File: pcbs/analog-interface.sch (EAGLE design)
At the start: 26 parts, among them U1 ISL3179EIBZ, U2 ATMEGA328P, U3 LM4120

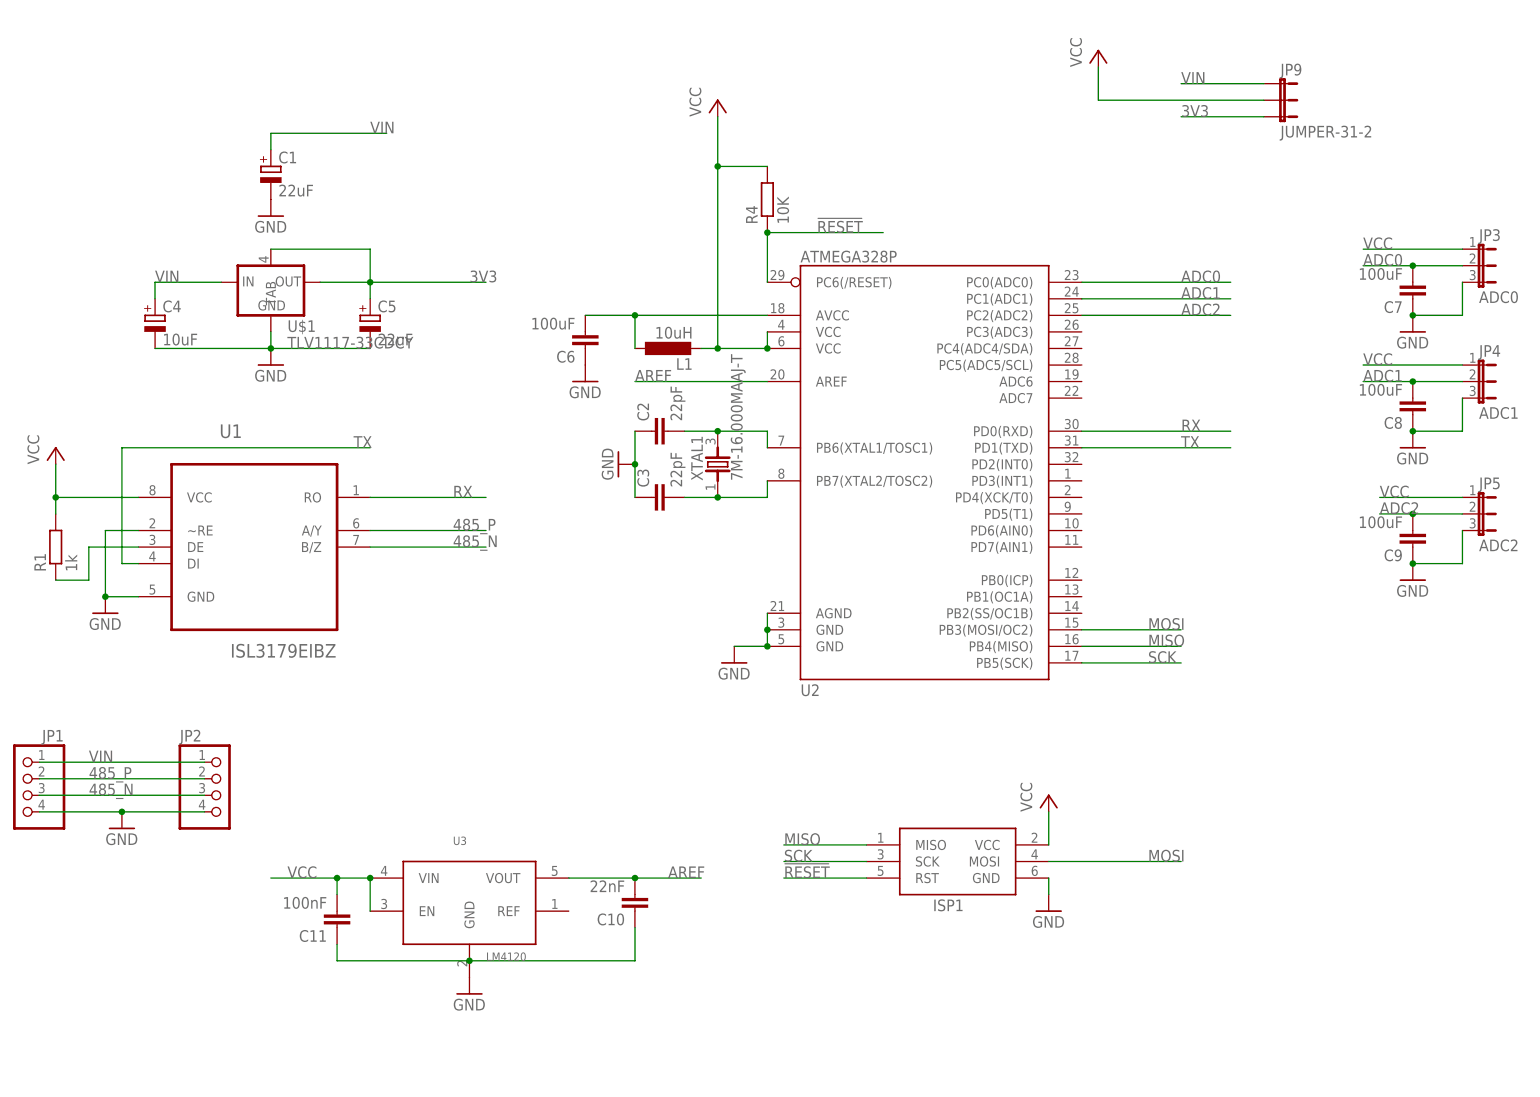
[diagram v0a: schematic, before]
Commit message: Now uses external ADC and is long and thin.  Possibly too long...
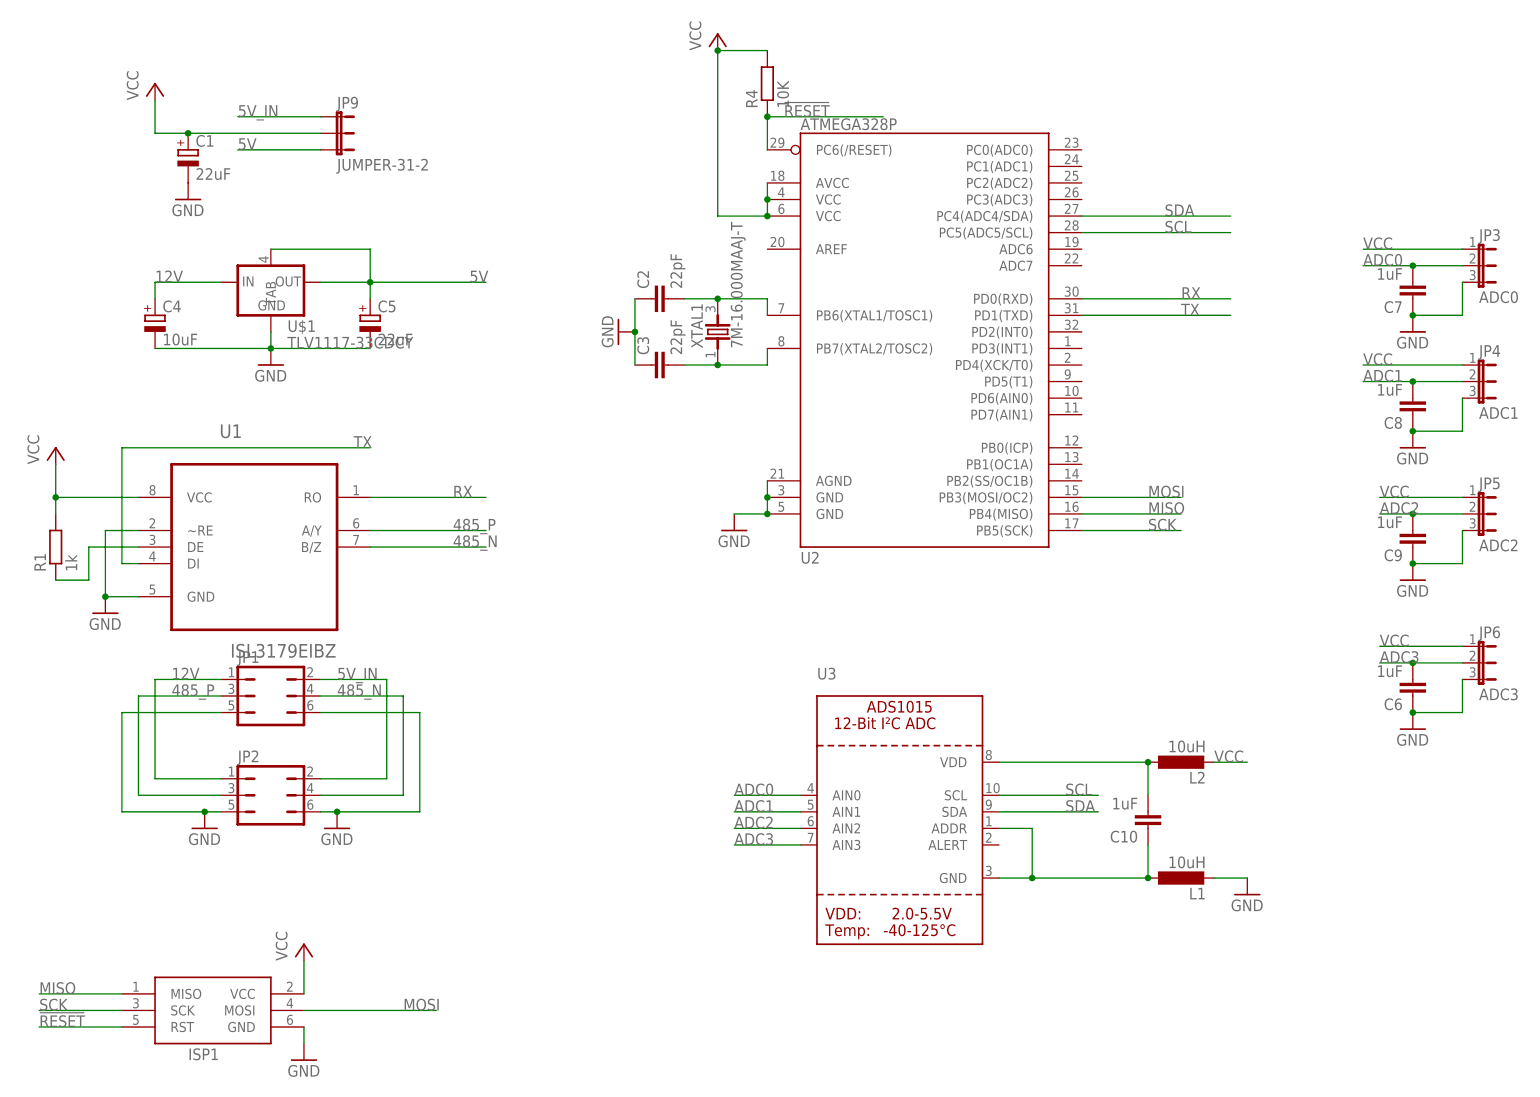
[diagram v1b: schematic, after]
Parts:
- removed C11: 100nF, resistor:C-EUC0805
- added JP6: ADC3, jumper:JP2E
- added L2: 10uH, resistor:L-EUL3216C
- C10: value 22nF -> 1uF
- C6, C7, C8, C9: value 100uF -> 1uF
- JP1, JP2: device pinhead:PINHD-1X4 -> jumper:JP3Q
- JP3, JP4, JP5: device farnell-parts:3-PIN-MOLEX -> jumper:JP2E
- U3: value LM4120 -> (none); device mountainsensing:LM4120 -> microbuilder:ADC_ADS1015
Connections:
- net 3V3 renamed 5V
- removed net AREF: C10.2, U2.AREF, U3.VOUT
- removed net VIN: C1.+, C4.+, JP1.1, JP2.1, JP9.1, U$1.IN
- new net 12V: C4.+, JP1.1, JP2.1, U$1.IN
- new net 5V_IN: JP1.2, JP2.2, JP9.1
- new net ADC3: C6.2, JP6.2, U3.AIN3
- new net SCL: U2.PC5(ADC5/SCL), U3.SCL
- new net SDA: U2.PC4(ADC4/SDA), U3.SDA
- net 485_N: now also JP1.4, JP2.4; no longer JP1.3, JP2.3
- net 485_P: now also JP1.3, JP2.3; no longer JP1.2, JP2.2
- net ADC0: now also U3.AIN0; no longer U2.PC0(ADC0)
- net ADC1: now also U3.AIN1; no longer U2.PC1(ADC1)
- net ADC2: now also U3.AIN2; no longer U2.PC2(ADC2)
- net GND: now also JP1.5, JP1.6, JP2.5, JP2.6, JP6.3, L1.2; no longer JP1.4, JP2.4, U3.GND
- net N$4: now also C10.1, U3.ADDR, U3.GND; no longer C6.2, U2.AVCC
- net N$7: now also C10.2, L2.1, U3.VDD; no longer C10.1, C11.1
- net VCC: now also C1.+, JP6.1, L2.2, U2.AVCC; no longer C11.2, L1.2, U3.EN, U3.VIN
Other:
- moved on the sheet: C1, C10, C2, C3, C6, ISP1, JP9, L1, R4, U2, XTAL1

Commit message: Now has seperate AGND and AVCC 12V available on ADC headers lots of vias A bit shorter
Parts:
- removed JP1, JP2: (no value), jumper:JP3Q
- added JP7, JP8: (no value), SparkFun-Connectors:M05PTH
- JP3: value ADC0 -> 0; device jumper:JP2E -> jumper:JP4E
- JP4: value ADC1 -> 1; device jumper:JP2E -> jumper:JP4E
- JP5: value ADC2 -> 2; device jumper:JP2E -> jumper:JP4E
- JP6: value ADC3 -> 3; device jumper:JP2E -> jumper:JP4E
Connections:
- removed net 12V: C4.+, JP1.1, JP2.1, U$1.IN
- removed net N$4: C10.1, L1.1, U3.ADDR, U3.GND
- removed net N$7: C10.2, L2.1, U3.VDD
- new net 12V_IN: C4.+, JP3.1, JP4.1, JP5.1, JP6.1, JP7.1, JP8.1, U$1.IN
- new net AGND: C10.1, C6.1, C7.1, C8.1, C9.1, JP3.4, JP4.4, JP5.4, JP6.4, L1.1, U3.ADDR, U3.GND
- new net AVCC: C10.2, JP3.2, JP4.2, JP5.2, JP6.2, L2.1, U3.VDD
- net 485_N: now also JP7.4, JP8.4; no longer JP1.4, JP2.4
- net 485_P: now also JP7.3, JP8.3; no longer JP1.3, JP2.3
- net 5V_IN: now also JP7.2, JP8.2; no longer JP1.2, JP2.2
- net ADC0: now also JP3.3; no longer JP3.2
- net ADC1: now also JP4.3; no longer JP4.2
- net ADC2: now also JP5.3; no longer JP5.2
- net ADC3: now also JP6.3; no longer JP6.2
- net GND: now also JP7.5, JP8.5; no longer C6.1, C7.1, C8.1, C9.1, JP1.5, JP1.6, JP2.5, JP2.6, JP3.3, JP4.3, JP5.3, JP6.3
- net VCC: no longer JP3.1, JP4.1, JP5.1, JP6.1
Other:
- moved on the sheet: C7, C8

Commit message: Pull ups added to I2C
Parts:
- added R2, R3: 1k, resistor:R-EU_R0805
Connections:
- net SCL: now also R2.1
- net SDA: now also R3.1
- net VCC: now also R2.2, R3.2
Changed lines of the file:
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@@
 <?xml version="1.0" encoding="utf-8"?>
 <!DOCTYPE eagle SYSTEM "eagle.dtd">
-<eagle version="6.6.0">
+<eagle version="6.5.0">
 <drawing>
 <settings>
@@
 <part name="JP8" library="SparkFun-Connectors" deviceset="M05" device="PTH"/>
 <part name="GND6" library="supply1" deviceset="GND" device=""/>
+<part name="R2" library="resistor" deviceset="R-EU_" device="R0805" value="1k"/>
+<part name="R3" library="resistor" deviceset="R-EU_" device="R0805" value="1k"/>
 </parts>
 <sheets>
@@
 <instance part="JP8" gate="G$1" x="17.78" y="53.34" rot="MR180"/>
 <instance part="GND6" gate="1" x="33.02" y="45.72"/>
+<instance part="R2" gate="G$1" x="180.34" y="149.86" rot="R90"/>
+<instance part="R3" gate="G$1" x="187.96" y="149.86" rot="R90"/>
 </instances>
 <busses>
@@
 <wire x1="121.92" y1="144.78" x2="121.92" y2="147.32" width="0.1524" layer="91"/>
 <junction x="121.92" y="144.78"/>
+<pinref part="R2" gate="G$1" pin="2"/>
+<wire x1="121.92" y1="167.64" x2="180.34" y2="167.64" width="0.1524" layer="91"/>
+<wire x1="180.34" y1="167.64" x2="180.34" y2="154.94" width="0.1524" layer="91"/>
+<pinref part="R3" gate="G$1" pin="2"/>
+<wire x1="180.34" y1="154.94" x2="187.96" y2="154.94" width="0.1524" layer="91"/>
+<junction x="180.34" y="154.94"/>
 </segment>
 <segment>
@@
 <segment>
 <pinref part="U2" gate="G$1" pin="PC5(ADC5/SCL)"/>
-<wire x1="170.18" y1="139.7" x2="193.04" y2="139.7" width="0.1524" layer="91"/>
+<wire x1="170.18" y1="139.7" x2="180.34" y2="139.7" width="0.1524" layer="91"/>
 <label x="182.88" y="139.7" size="1.778" layer="95"/>
+<pinref part="R2" gate="G$1" pin="1"/>
+<wire x1="180.34" y1="139.7" x2="193.04" y2="139.7" width="0.1524" layer="91"/>
+<wire x1="180.34" y1="144.78" x2="180.34" y2="139.7" width="0.1524" layer="91"/>
+<junction x="180.34" y="139.7"/>
 </segment>
 <segment>
@@
 <segment>
 <pinref part="U2" gate="G$1" pin="PC4(ADC4/SDA)"/>
-<wire x1="170.18" y1="142.24" x2="193.04" y2="142.24" width="0.1524" layer="91"/>
+<wire x1="170.18" y1="142.24" x2="187.96" y2="142.24" width="0.1524" layer="91"/>
 <label x="182.88" y="142.24" size="1.778" layer="95"/>
-</segment>
-<segment>
+<pinref part="R3" gate="G$1" pin="1"/>
+<wire x1="187.96" y1="142.24" x2="193.04" y2="142.24" width="0.1524" layer="91"/>
+<wire x1="187.96" y1="144.78" x2="187.96" y2="142.24" width="0.1524" layer="91"/>
+<junction x="187.96" y="142.24"/>
+</segment>
+<segment>

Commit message: Now has control of Tx/Rx for RS485 chip
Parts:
- removed R1: 1k, resistor:R-EU_R0805
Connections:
- removed net N$1: R1.1, U1.DE
- new net TXEN: U1.DE, U1.~RE, U2.PD2(INT0)
- net GND: no longer U1.~RE
- net VCC: no longer R1.2
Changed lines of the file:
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@@
 <?xml version="1.0" encoding="utf-8"?>
 <!DOCTYPE eagle SYSTEM "eagle.dtd">
-<eagle version="6.5.0">
+<eagle version="6.6.0">
 <drawing>
 <settings>
@@
 <part name="C1" library="resistor" deviceset="CPOL-EU" device="A/3216-18R" value="22uF"/>
 <part name="GND3" library="supply1" deviceset="GND" device=""/>
-<part name="R1" library="resistor" deviceset="R-EU_" device="R0805" value="1k"/>
 <part name="ISP1" library="adafruit" deviceset="AVRISP" device="-6"/>
 <part name="P+2" library="glacsweb" deviceset="VCC" device=""/>
@@
 <instance part="C1" gate="G$1" x="33.02" y="152.4"/>
 <instance part="GND3" gate="1" x="20.32" y="81.28"/>
-<instance part="R1" gate="G$1" x="12.7" y="91.44" rot="R90"/>
 <instance part="ISP1" gate="G$1" x="35.56" y="20.32"/>
 <instance part="P+2" gate="VCC" x="50.8" y="30.48"/>
@@
 <net name="GND" class="0">
 <segment>
+<pinref part="GND3" gate="1" pin="GND"/>
 <pinref part="U1" gate="A" pin="GND"/>
-<pinref part="GND3" gate="1" pin="GND"/>
 <wire x1="25.4" y1="83.82" x2="20.32" y2="83.82" width="0.1524" layer="91"/>
-<pinref part="U1" gate="A" pin="~RE"/>
-<wire x1="25.4" y1="93.98" x2="20.32" y2="93.98" width="0.1524" layer="91"/>
-<wire x1="20.32" y1="93.98" x2="20.32" y2="83.82" width="0.1524" layer="91"/>
-<junction x="20.32" y="83.82"/>
 </segment>
 <segment>
@@
 <pinref part="U1" gate="A" pin="VCC"/>
 <wire x1="25.4" y1="99.06" x2="12.7" y2="99.06" width="0.1524" layer="91"/>
-<pinref part="R1" gate="G$1" pin="2"/>
-<wire x1="12.7" y1="96.52" x2="12.7" y2="99.06" width="0.1524" layer="91"/>
-<junction x="12.7" y="99.06"/>
 </segment>
 <segment>
@@
 </segment>
 </net>
-<net name="N$1" class="0">
-<segment>
-<pinref part="U1" gate="A" pin="DE"/>
-<wire x1="25.4" y1="91.44" x2="17.78" y2="91.44" width="0.1524" layer="91"/>
-<wire x1="17.78" y1="91.44" x2="17.78" y2="86.36" width="0.1524" layer="91"/>
-<pinref part="R1" gate="G$1" pin="1"/>
-<wire x1="17.78" y1="86.36" x2="12.7" y2="86.36" width="0.1524" layer="91"/>
-</segment>
-</net>
 <net name="!RESET" class="0">
 <segment>
@@
 </segment>
 </net>
+<net name="TXEN" class="0">
+<segment>
+<pinref part="U1" gate="A" pin="DE"/>
+<wire x1="25.4" y1="91.44" x2="10.16" y2="91.44" width="0.1524" layer="91"/>
+<pinref part="U1" gate="A" pin="~RE"/>
+<wire x1="25.4" y1="91.44" x2="25.4" y2="93.98" width="0.1524" layer="91"/>
+<junction x="25.4" y="91.44"/>
+<label x="10.16" y="91.44" size="1.778" layer="95"/>
+</segment>
+<segment>
+<pinref part="U2" gate="G$1" pin="PD2(INT0)"/>
+<wire x1="170.18" y1="124.46" x2="193.04" y2="124.46" width="0.1524" layer="91"/>
+<label x="185.42" y="124.46" size="1.778" layer="95"/>
+</segment>
+</net>
